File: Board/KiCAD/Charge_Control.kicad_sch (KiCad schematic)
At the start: 56 parts, among them Q1 AONR32320C, Q10 AON7407, Q2 AONR32320C, Q3 AONR32320C, Q4 AONR32320C, U1 BQ25730RSNR, U3 LTC2943CDD#PBF

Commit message: PCB Optimization
Made changes to the PCB to make it smaller, as well as adding the Castellated Vias

@andrewgreenberg
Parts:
- TP2, TP27, TP28, TP3, TP4, TP5: footprint TestPoint:TestPoint_THTPad_1.0x1.0mm_Drill0.5mm -> TestPoint:TestPoint_Pad_1.0x1.0mm
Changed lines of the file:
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@@
 			)
 		)
-		(property "Footprint" "TestPoint:TestPoint_THTPad_1.0x1.0mm_Drill0.5mm"
+		(property "Footprint" "TestPoint:TestPoint_Pad_1.0x1.0mm"
 			(at 167.64 130.81 0)
 			(effects
@@
 			)
 		)
-		(property "Footprint" "TestPoint:TestPoint_THTPad_1.0x1.0mm_Drill0.5mm"
+		(property "Footprint" "TestPoint:TestPoint_Pad_1.0x1.0mm"
 			(at 80.01 133.35 0)
 			(effects
@@
 			)
 		)
-		(property "Footprint" "TestPoint:TestPoint_THTPad_1.0x1.0mm_Drill0.5mm"
+		(property "Footprint" "TestPoint:TestPoint_Pad_1.0x1.0mm"
 			(at 144.78 146.05 0)
 			(effects
@@
 			)
 		)
-		(property "Footprint" "TestPoint:TestPoint_THTPad_1.0x1.0mm_Drill0.5mm"
+		(property "Footprint" "TestPoint:TestPoint_Pad_1.0x1.0mm"
 			(at 121.92 50.8 0)
 			(effects
@@
 			)
 		)
-		(property "Footprint" "TestPoint:TestPoint_THTPad_1.0x1.0mm_Drill0.5mm"
+		(property "Footprint" "TestPoint:TestPoint_Pad_1.0x1.0mm"
 			(at 139.7 50.8 0)
 			(effects
@@
 			)
 		)
-		(property "Footprint" "TestPoint:TestPoint_THTPad_1.0x1.0mm_Drill0.5mm"
+		(property "Footprint" "TestPoint:TestPoint_Pad_1.0x1.0mm"
 			(at 130.81 135.89 0)
 			(effects

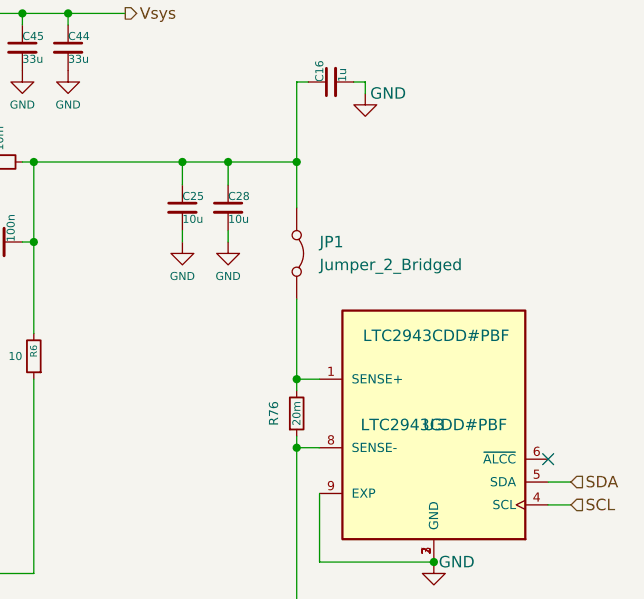
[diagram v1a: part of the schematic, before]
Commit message: Cleaned up BOM materials again. Why do these keep reseting? Also, big refactor on cell balancing circuits and battery connection (NOW FLIPPED) to make board smaller. More smallification is left as an exercise to the reader.
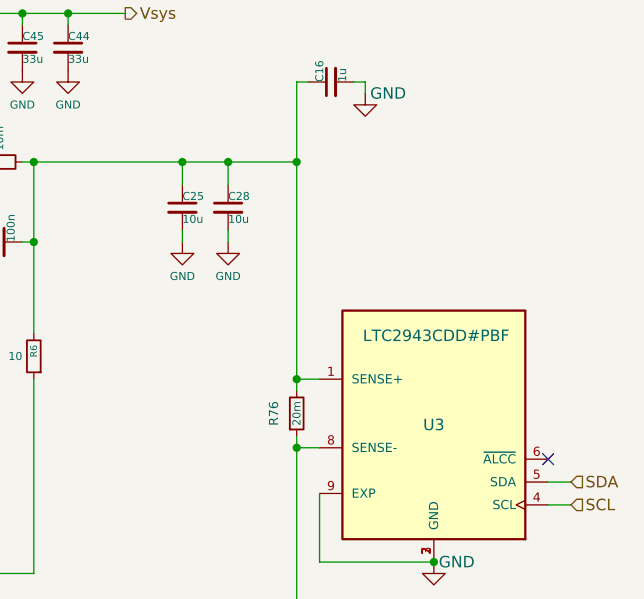
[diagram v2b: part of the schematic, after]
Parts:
- removed JP1: Jumper_2_Bridged, TestPoint:TestPoint_2Pads_Pitch2.54mm_Drill0.8mm, symbol Jumper:Jumper_2_Bridged
- C10, C12, C22, C25, C28, C29: Package CL31B106KAHNNNE -> (none)
- C13, C16, C40: Package 0603B105K100XD -> (none)
- C14, C15: Package GCM188R71H473KA55D -> (none)
- C23: Package CL05B104KA5NNNC -> (none)
- C26: Package CL10A335KP8NNNC -> (none)
- C27, C35: Package GRM1885C1H101JA01D -> (none)
- C37: Package 600S150JT250XT4K -> (none)
- C38: Package CGA3E2C0G1H472J080AA -> (none)
- C39: Package C0603C681F5GACTU -> (none)
- C41, C9: Package GRM033R71A103KA01D -> (none)
- C42, C43: Package GCM188R71H333KA55D -> (none)
- C44, C45: Package GRM1885C1H330JA01D -> (none)
- L2: Package B82464G4472M000 -> (none)
- Q1, Q2, Q3, Q4: Package AONR32320C -> (none)
- Q10: Package AON7407 -> (none)
- R10, R5, R6: Package RMCF0603FT10R0 -> (none)
- R15: Package RMCF0603FT10K0 -> (none)
- R2, R4: Package CSR1206FK10L0 -> (none)
- R3: Package RMCF1206FT2R20 -> (none)
- R36: Package RMCF0603FT15K0CT-ND -> (none)
- R37: Package RMCF0603JT39K0 -> (none)
- R38: Package RMCF0603FT220K -> (none)
- R39: Package RMCF0603FT383K -> (none)
- R41, R42: Package RMCF0603FT5R10 -> (none)
- R7: Package RMCF0603FT33K0 -> (none)
- R76: Package CSR1206FK20L0 -> (none)
- R9: Package RMCF0603FT187K -> (none)
- U1: Package BQ25730RSNR -> (none)
- U3: Package LTC2943CDD#PBF -> (none)
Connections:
- net at C16.1, C23.2, C25.1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: now also R76.2, U3.1 (SENSE+)

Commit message: PCB with updated Footprint for LTC
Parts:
- U3: footprint Package_SO:SOIC-8-1EP_3.9x4.9mm_P1.27mm_EP2.29x3mm -> Package_DFN_QFN:MLF-8-1EP_3x3mm_P0.65mm_EP1.55x2.3mm
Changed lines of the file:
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@@
 			)
 		)
-		(property "Footprint" "Package_SO:SOIC-8-1EP_3.9x4.9mm_P1.27mm_EP2.29x3mm"
+		(property "Footprint" "Package_DFN_QFN:MLF-8-1EP_3x3mm_P0.65mm_EP1.55x2.3mm"
 			(at 242.57 80.01 0)
 			(effects
